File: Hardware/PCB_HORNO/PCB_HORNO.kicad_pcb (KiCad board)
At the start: 2 copper layers, 273 parts, among them J0_1 Screw_Terminal_01x03, J0_10 Screw_Terminal_01x03, J0_13 Screw_Terminal_01x03, J0_14 Screw_Terminal_01x03, J0_16 Screw_Terminal_01x03, J0_18 Screw_Terminal_01x03, J0_19 Screw_Terminal_01x03, J0_2 Screw_Terminal_01x03, J0_20 Screw_Terminal_01x03, J0_21 Screw_Terminal_01x03, J0_22 Screw_Terminal_01x03, J0_23 Screw_Terminal_01x03, J0_24 Screw_Terminal_01x03, J0_25 Screw_Terminal_01x03, J0_26 Screw_Terminal_01x03, J0_3 Screw_Terminal_01x03, J0_5 Screw_Terminal_01x03, J0_6 Screw_Terminal_01x03, J0_7 Screw_Terminal_01x03, J0_8 Screw_Terminal_01x03, J0_9 Screw_Terminal_01x03, J1 Screw_Terminal_01x20, J2 Screw_Terminal_01x20, J3 Screw_Terminal_01x20, J4 Screw_Terminal_01x20, K1 Fujitsu_FTR-LYCA005x, K2 Fujitsu_FTR-LYCA005x, K3 Fujitsu_FTR-LYCA005x, K4 Fujitsu_FTR-LYCA005x, Q1 2N2222, Q2 2N2222, Q3 2N2222, Q4 2N2222, Q5 BTA16-800B, Q6 IRG4PF50W, Q7 IRG4PF50W, U1 TLP521-1, U10 LM741, U11 LM741, U12 LM741, U13 MOC3021M, U14 TLP521-1, U15 TLP250, U16 TLP521-1, U17 LM741, U18 LM741, U19 TLP250, U2 TLP521-1, U20 L298HN, U21 TLP521-1, U22 TLP521-1, U23 TLP521-1, U3 TLP521-1, U4 TLP521-1, U5 TLP521-1, U6 TLP521-1, U7 TLP521-1, U8 TLP521-1, U9 LM741

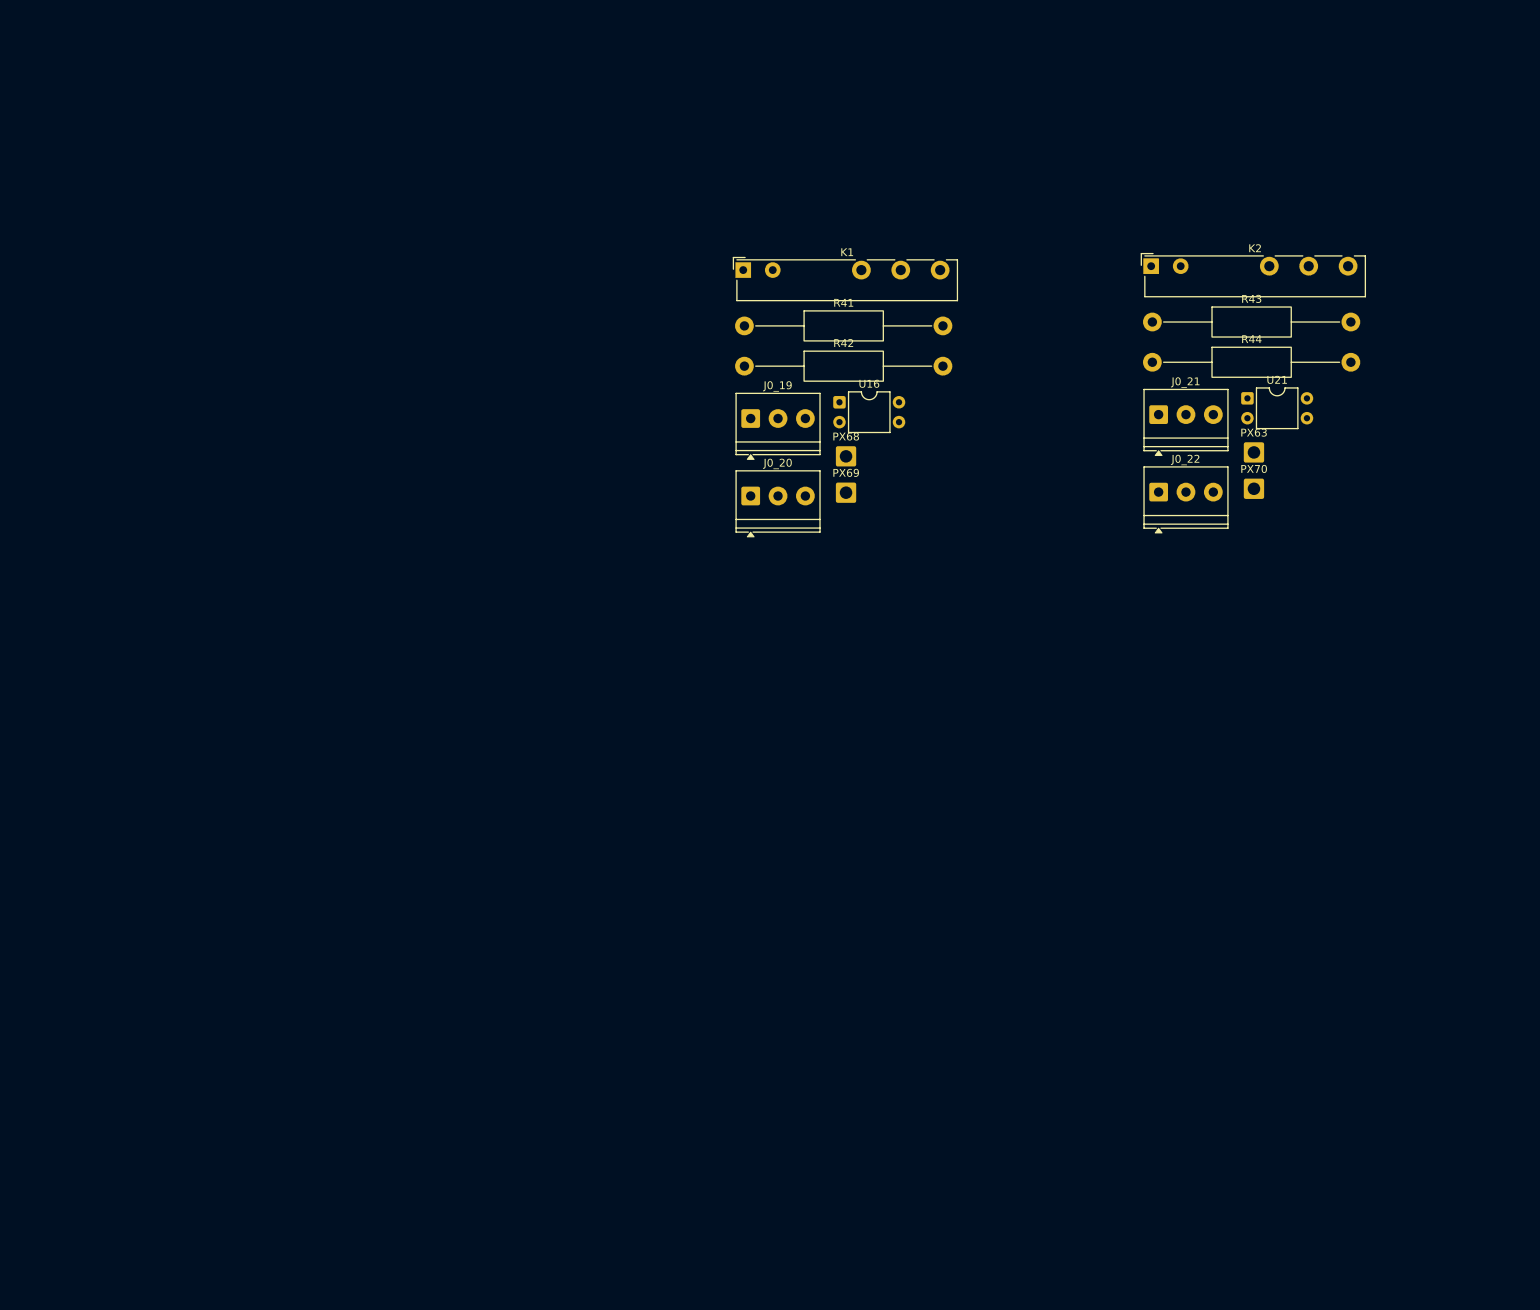
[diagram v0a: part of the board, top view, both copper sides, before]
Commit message: Agregando diodos de rueda libre (flyback)
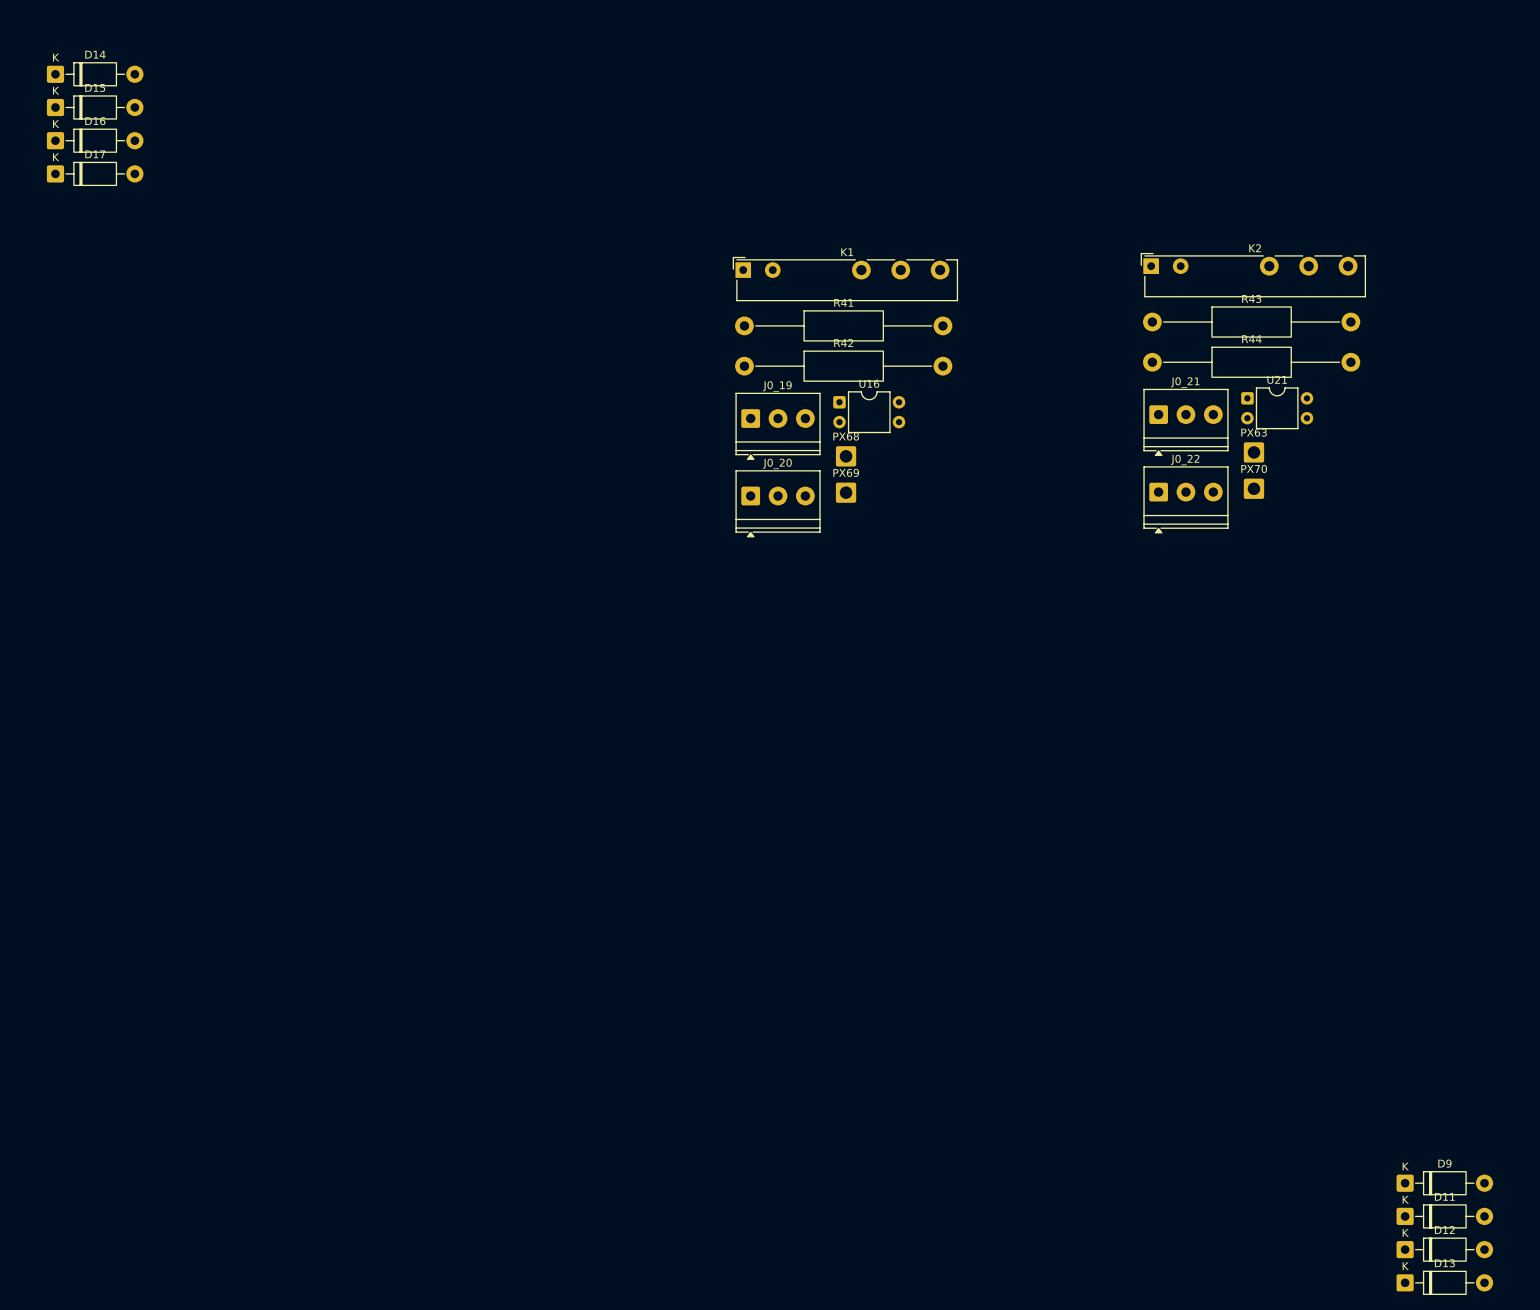
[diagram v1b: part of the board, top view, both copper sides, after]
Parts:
- added D11: 1N4007, Diode_THT:D_DO-41_SOD81_P10.16mm_Horizontal, F.Cu at (146.5, 530.1)
- added D12: 1N4007, Diode_THT:D_DO-41_SOD81_P10.16mm_Horizontal, F.Cu at (146.5, 534.4)
- added D13: 1N4007, Diode_THT:D_DO-41_SOD81_P10.16mm_Horizontal, F.Cu at (146.5, 538.6)
- added D14: 1N4007, Diode_THT:D_DO-41_SOD81_P10.16mm_Horizontal, F.Cu at (-26.2, 383.9)
- added D15: 1N4007, Diode_THT:D_DO-41_SOD81_P10.16mm_Horizontal, F.Cu at (-26.2, 388.2)
- added D16: 1N4007, Diode_THT:D_DO-41_SOD81_P10.16mm_Horizontal, F.Cu at (-26.2, 392.4)
- added D17: 1N4007, Diode_THT:D_DO-41_SOD81_P10.16mm_Horizontal, F.Cu at (-26.2, 396.7)
- added D9: 1N4007, Diode_THT:D_DO-41_SOD81_P10.16mm_Horizontal, F.Cu at (146.5, 525.9)

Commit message: PCB preliminar
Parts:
- RV1: value R_Potentiometer_US -> Potentiometer
- moved J0_5 336.8 mm to (892.9, 343.2), turned to 90 degrees
- moved J0_6 334.0 mm to (892.6, 366.8), turned to 90 degrees
- moved D14 327.8 mm to (297.8, 334.1), turned to 180 degrees
- moved D15 317.8 mm to (287.6, 338.1)
- moved U9 306.7 mm to (836.6, 327.8)
- moved J0_16 305.0 mm to (314.9, 350.4)
- moved C5 304.8 mm to (864.6, 339.4), turned to 90 degrees
- moved D16 304.2 mm to (272.4, 334.2), turned to 180 degrees
- moved C6 302.4 mm to (864.3, 351.5), turned to 90 degrees
- moved C4 295.0 mm to (863.9, 370.8), turned to 90 degrees
- moved D17 294.3 mm to (262.2, 338.1)
- moved J0_10 293.9 mm to (289.3, 350.4)
- moved U10 293.4 mm to (837.4, 344.7)
- moved C10 292.8 mm to (270.3, 304.4)
- moved C11 292.8 mm to (270.3, 312.4)
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
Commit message: Esquematico definitivo
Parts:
- removed D14, D15, D16, D17: 1N4007, Diode_THT:D_DO-41_SOD81_P10.16mm_Horizontal

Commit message: Actualización de esquematico
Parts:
- removed PX116, PX120, PX56, PX58, PX60, PX61, PX64, PX65, PX68, PX70, PX71, PX73, PX74, PX75, PX76, PX77, PX78, PX79, PX81, PX82, PX83, PX84, PX85, PX86, PX87, PX88, PX89, PX90: ~, Connector_Wire:SolderWire-0.75sqmm_1x01_D1.25mm_OD2.3mm
- R1, R12, R14, R15, R16, R17, R18, R19, R2, R20, R21, R22, R23, R24, R25, R26, R3, R35, R36, R37, R38, R4, R41, R44, R46, R48, R49, R5, R6, R7, R8: footprint Resistor_THT:R_Axial_DIN0411_L9.9mm_D3.6mm_P25.40mm_Horizontal -> Resistor_THT:R_Axial_DIN0207_L6.3mm_D2.5mm_P10.16mm_Horizontal
- R13, R27, R28, R29, R30, R31, R32, R33, R34, R39, R40, R42, R43, R45, R47: footprint Resistor_THT:R_Axial_DIN0411_L9.9mm_D3.6mm_P25.40mm_Horizontal -> Resistor_THT:R_Axial_DIN0309_L9.0mm_D3.2mm_P15.24mm_Horizontal
- RV1: value Potentiometer -> R_Potentiometer_US
- moved PX45 641.0 mm to (272.9, 274.6)
- moved J0_5 554.8 mm to (395.6, 97.3), turned to 180 degrees
- moved J0_6 544.6 mm to (419.2, 97.6), turned to 180 degrees
- moved PX55 489.3 mm to (277.5, 274.6)
- moved C3 480.0 mm to (444.7, 151.3), turned to -90 degrees
- moved C4 466.8 mm to (445.0, 165.0), turned to -90 degrees
- moved C6 451.8 mm to (444.6, 184.3), turned to -90 degrees
- moved C5 444.0 mm to (444.3, 196.4), turned to -90 degrees
- moved J0_3 436.5 mm to (-361.2, 28.9), turned to 180 degrees
- moved U12 435.3 mm to (471.0, 150.8), turned to 180 degrees
- moved J0_2 433.9 mm to (-340.9, 28.9), turned to 180 degrees
- moved J0_1 432.8 mm to (-318.7, 29.2), turned to 180 degrees
- moved U11 412.7 mm to (471.4, 172.6), turned to 180 degrees
- moved U10 396.9 mm to (471.5, 191.1), turned to 180 degrees
- moved U9 383.6 mm to (472.2, 208.0), turned to 180 degrees
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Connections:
- C10 pad 1: Net-(J0_16-Pin_1) -> Net-(GND1-Pin_1)
- C11 pad 1: Net-(J0_16-Pin_1) -> Net-(GND1-Pin_1)
- C3 pad 2: Net-(J0_6-Pin_2) -> Net-(GND1-Pin_1)
- C4 pad 2: Net-(J0_6-Pin_2) -> Net-(GND1-Pin_1)
- C5 pad 2: Net-(J0_6-Pin_2) -> Net-(GND1-Pin_1)
- C6 pad 2: Net-(J0_6-Pin_2) -> Net-(GND1-Pin_1)
- C8 pad 2: Net-(J0_6-Pin_2) -> Net-(GND1-Pin_1)
- C9 pad 2: Net-(J0_6-Pin_2) -> Net-(GND1-Pin_1)
- J0_16 pad 1: Net-(J0_16-Pin_1) -> Net-(GND1-Pin_1)
- J0_6 pad 2: Net-(J0_6-Pin_2) -> Net-(GND1-Pin_1)
- J0_6 pad 3: Net-(J0_6-Pin_2) -> Net-(GND1-Pin_1)
- PS1 pad 1: Net-(PS1--Vin) -> Net-(GND1-Pin_1)
- PS1 pad 2: Net-(PS1-+Vin) -> Net-(5Vb1-Pin_1)
- PS2 pad 1: Net-(PS2--Vin) -> Net-(GND1-Pin_1)
- PS2 pad 2: Net-(PS2-+Vin) -> Net-(5Vb1-Pin_1)
- PS3 pad 1: Net-(PS3--Vin) -> Net-(GND1-Pin_1)
- PS3 pad 2: Net-(PS3-+Vin) -> Net-(5Vb1-Pin_1)
- PS4 pad 1: Net-(PS4--Vin) -> Net-(GND1-Pin_1)
- PS4 pad 2: Net-(PS4-+Vin) -> Net-(5Vb1-Pin_1)
- PS5 pad 1: Net-(PS5--Vin) -> Net-(GND1-Pin_1)
- PS5 pad 2: Net-(PS5-+Vin) -> Net-(3V3a1-Pin_1)
- PS5 pad 3: Net-(PS5--Vout) -> Net-(GND1-Pin_1)
- PS6 pad 1: Net-(PS6--Vin) -> Net-(GND1-Pin_1)
- PS6 pad 2: Net-(PS6-+Vin) -> Net-(5Vb1-Pin_1)
- PS6 pad 3: Net-(J0_6-Pin_2) -> Net-(GND1-Pin_1)
- PS7 pad 1: Net-(PS7--Vin) -> Net-(GND1-Pin_1)
- PS7 pad 2: Net-(PS7-+Vin) -> Net-(5Vb1-Pin_1)
- PS7 pad 4: Net-(J0_6-Pin_2) -> Net-(GND1-Pin_1)
- PS8 pad 1: Net-(PS8--Vin) -> Net-(GND1-Pin_1)
- PS8 pad 2: Net-(PS8-+Vin) -> Net-(5Vb1-Pin_1)
- PS8 pad 3: Net-(J0_6-Pin_2) -> Net-(GND1-Pin_1)
- PX45 pad 1: Net-(PS5--Vout) -> Net-(PX45-Pin_1)
- PX46 pad 1: Net-(PS5--Vout) -> Net-(GND1-Pin_1)
- PX55 pad 1: Net-(PS5--Vout) -> Net-(PX55-Pin_1)
- R1 pad 1: Net-(PS5--Vout) -> Net-(GND1-Pin_1)
- R1 pad 2: Net-(PS5--Vout) -> Net-(GND1-Pin_1)
- R2 pad 2: Net-(PS5--Vout) -> Net-(GND1-Pin_1)
- R21 pad 2: Net-(J0_6-Pin_2) -> Net-(GND1-Pin_1)
- R23 pad 2: Net-(J0_6-Pin_2) -> Net-(GND1-Pin_1)
- R3 pad 2: Net-(PS5--Vout) -> Net-(GND1-Pin_1)
- R35 pad 2: Net-(J0_6-Pin_2) -> Net-(GND1-Pin_1)
- R36 pad 2: Net-(J0_6-Pin_2) -> Net-(GND1-Pin_1)
- R37 pad 2: Net-(J0_6-Pin_2) -> Net-(GND1-Pin_1)
- R38 pad 2: Net-(J0_6-Pin_2) -> Net-(GND1-Pin_1)
- R39 pad 1: Net-(J0_16-Pin_1) -> Net-(GND1-Pin_1)
- R4 pad 2: Net-(PS5--Vout) -> Net-(GND1-Pin_1)
- R40 pad 1: Net-(J0_16-Pin_1) -> Net-(GND1-Pin_1)
- R5 pad 2: Net-(PS5--Vout) -> Net-(GND1-Pin_1)
- R6 pad 2: Net-(PS5--Vout) -> Net-(GND1-Pin_1)
- R7 pad 2: Net-(PS5--Vout) -> Net-(GND1-Pin_1)
- R8 pad 2: Net-(PS5--Vout) -> Net-(GND1-Pin_1)
- RV1 pad 1: Net-(PX58-Pin_1) -> Net-(GND1-Pin_1)
- RV1 pad 3: Net-(PX60-Pin_1) -> Net-(3V3a1-Pin_1)
- U1 pad 3: Net-(PS5--Vout) -> Net-(GND1-Pin_1)
- U13 pad 2: Net-(PX56-Pin_1) -> Net-(GND1-Pin_1)
- U14 pad 3: Net-(PS5--Vout) -> Net-(GND1-Pin_1)
- U15 pad 3: Net-(PX65-Pin_1) -> Net-(GND1-Pin_1)
- U16 pad 2: Net-(PX68-Pin_1) -> Net-(GND1-Pin_1)
- U19 pad 3: Net-(PX79-Pin_1) -> Net-(GND1-Pin_1)
- U20 pad 11: unconnected-(U20-EnB-Pad11) -> Net-(PX45-Pin_1)
- U20 pad 6: unconnected-(U20-EnA-Pad6) -> Net-(PX55-Pin_1)
- U20 pad 8: Net-(J0_16-Pin_1) -> Net-(GND1-Pin_1)
- U21 pad 2: Net-(PX70-Pin_1) -> Net-(GND1-Pin_1)
- U22 pad 2: Net-(PX64-Pin_1) -> Net-(GND1-Pin_1)
- U23 pad 2: Net-(PX71-Pin_1) -> Net-(GND1-Pin_1)

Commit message: Actualización de PCB
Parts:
- moved PX118 560.0 mm to (188.1, 118.3), turned to 180 degrees
- moved PX119 556.1 mm to (188.1, 112.8), turned to 180 degrees
- moved R23 531.2 mm to (221.2, 138.7), turned to 90 degrees
- moved R49 530.2 mm to (89.9, 92.7), turned to 180 degrees
- moved C9 520.5 mm to (207.8, 120.5), turned to -90 degrees
- moved U18 507.5 mm to (206.8, 107.6), turned to 90 degrees
- moved R24 502.4 mm to (220.8, 121.2), turned to 90 degrees
- moved R21 498.9 mm to (252.5, 139.7), turned to 90 degrees
- moved R8 494.7 mm to (92.2, 180.5), turned to 0 degrees
- moved PS7 490.3 mm to (221.9, 90.9)
- moved PS8 490.3 mm to (200.0, 91.0)
- moved PS6 490.3 mm to (242.0, 91.3)
- moved C8 488.9 mm to (236.1, 124.4), turned to -90 degrees
- moved PX53 488.9 mm to (109.2, 160.6), turned to 0 degrees
- moved PX52 485.5 mm to (109.2, 156.0), turned to 0 degrees
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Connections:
- J0_13 pad 2: unconnected-(J0_13-Pin_2-Pad2) -> Net-(GND1-Pin_1)
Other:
- board outline added: 256.1 x 296.8 mm

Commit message: Layout del PCB
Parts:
- added REF**: MountingHole_4.5mm_Pad, MountingHole:MountingHole_4.5mm_Pad, F.Cu at (44.5, 268.0)
- added REF**: MountingHole_4.5mm_Pad, MountingHole:MountingHole_4.5mm_Pad, F.Cu at (254.0, 268.0)
- added REF**: MountingHole_4.5mm_Pad, MountingHole:MountingHole_4.5mm_Pad, F.Cu at (254.0, 21.0)
- added REF**: MountingHole_4.5mm_Pad, MountingHole:MountingHole_4.5mm_Pad, F.Cu at (147.8, 117.0)
- added REF**: MountingHole_4.5mm_Pad, MountingHole:MountingHole_4.5mm_Pad, F.Cu at (44.5, 21.0)
- RV1: value R_Potentiometer_US -> Potentiometer
- moved J0_19 33.4 mm to (56.0, 262.8)
- moved J0_21 28.8 mm to (93.0, 262.8)
- moved J0_20 27.1 mm to (71.5, 262.8)
- moved J0_16 26.5 mm to (234.1, 262.7)
- moved K1 25.8 mm to (80.5, 249.8)
- moved D11 25.6 mm to (100.5, 228.8)
- moved J0_10 25.4 mm to (218.1, 262.7)
- moved J0_23 25.2 mm to (130.0, 262.8)
- moved R43 24.9 mm to (92.5, 239.8)
- moved U16 24.5 mm to (73.5, 231.8)
- moved R42 24.5 mm to (55.5, 239.8)
- moved J0_22 24.4 mm to (108.5, 262.8)
- moved R21 24.2 mm to (235.0, 123.0)
- moved J0_26 24.2 mm to (181.5, 262.8)
- moved U21 24.0 mm to (110.5, 231.8)
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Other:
- board size 256.1 x 296.8 mm -> 226.2 x 263.7 mm

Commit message: Ruteo
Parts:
- moved PX10 0.92 mm to (130.6, 146.7)
- moved PX11 0.92 mm to (130.6, 150.7)
- moved PX12 0.92 mm to (130.6, 154.7)
- moved PX13 0.92 mm to (130.6, 158.7)
- moved PX14 0.92 mm to (130.6, 162.7)
- moved PX15 0.92 mm to (130.6, 166.7)
- moved PX16 0.92 mm to (130.6, 170.7)
- moved PX17 0.92 mm to (130.6, 174.7)
- moved PX18 0.92 mm to (130.6, 178.7)
- moved PX19 0.92 mm to (130.6, 182.7)
- moved PX20 0.92 mm to (130.6, 186.7)
- moved PX21 0.92 mm to (130.6, 190.7)
- moved PX22 0.92 mm to (130.6, 194.7)
- moved PX6 0.92 mm to (130.6, 130.7)
- moved PX7 0.92 mm to (130.6, 134.7)
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- renumbered REF** to H1, REF** to H2, REF** to H3, REF** to H4, REF** to H5
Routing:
- net Net-(GND1-Pin_1): track 0.00 -> 1057.3 mm, vias 0 -> 1
- net Net-(5Vb1-Pin_1): track 0.00 -> 235.8 mm, vias 0 -> 1
- net Net-(3V3a1-Pin_1): track 0.00 -> 222.4 mm, vias 0 -> 1
- net Net-(PS6-+Vout): track 0.00 -> 153.5 mm, vias 0 -> 1
- net Net-(PS7--Vout): track 0.00 -> 140.7 mm, vias 0 -> 1
- net Net-(J0_1-Pin_1): track 0.00 -> 132.3 mm
- net Net-(R49-Pad2): track 0.00 -> 104.2 mm
- net Net-(J0_14-Pin_3): track 0.00 -> 90.4 mm
- net Net-(J0_18-Pin_3): track 0.00 -> 89.1 mm, vias 0 -> 1
- net Net-(J0_5-Pin_1): track 0.00 -> 82.2 mm
- net Net-(PS8-+Vout): track 0.00 -> 73.3 mm
- net Net-(J0_13-Pin_1): track 0.00 -> 69.8 mm, vias 0 -> 1
- net Net-(J0_5-Pin_2): track 0.00 -> 68.4 mm
- net Net-(J0_9-Pin_1): track 0.00 -> 67.2 mm, vias 0 -> 1
- net Net-(PS5-+Vout): track 0.00 -> 62.4 mm
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
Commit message: Ruteo de PCB
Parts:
- RV1: value Potentiometer -> R_Potentiometer_US
- moved PX62 21.5 mm to (237.0, 212.0)
- moved J0_6 19.4 mm to (251.9, 40.6)
- moved J0_5 19.4 mm to (252.0, 60.0)
- moved R40 17.1 mm to (200.6, 251.0)
- moved PX55 17.0 mm to (227.7, 212.0)
- moved U20 15.4 mm to (227.3, 243.7), turned to 0 degrees
- moved C11 15.4 mm to (210.3, 234.8)
- moved PX112 14.1 mm to (210.7, 212.0)
- moved PX113 14.1 mm to (215.3, 212.0)
- moved C5 14.0 mm to (207.0, 22.6)
- moved C6 14.0 mm to (193.0, 22.7)
- moved PX111 12.3 mm to (232.4, 212.0)
- moved R23 10.0 mm to (204.9, 113.0), turned to -90 degrees
- moved R24 10.0 mm to (204.9, 95.0), turned to -90 degrees
- moved R21 10.0 mm to (235.0, 113.0), turned to -90 degrees
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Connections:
- C2 pad 2: Net-(GND3-Pin_1) -> Net-(GND1-Pin_1)
- GND3 pad 1: Net-(GND3-Pin_1) -> Net-(GND1-Pin_1)
- J4 pad 20: Net-(GND3-Pin_1) -> Net-(GND1-Pin_1)
- PS8 pad 2: Net-(5Vb1-Pin_1) -> Net-(3V3b1-Pin_1)
- PX46 pad 1: Net-(GND1-Pin_1) -> Net-(PX46-Pin_1)
- R1 pad 1: Net-(GND1-Pin_1) -> Net-(PX46-Pin_1)
- U1 pad 3: Net-(GND1-Pin_1) -> Net-(PX46-Pin_1)
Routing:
- net Net-(GND1-Pin_1): track 1057.3 -> 1206.6 mm, vias 1 -> 3
- net Net-(PS6-+Vout): track 153.5 -> 217.4 mm, vias 1 -> 0
- net Net-(3V3b1-Pin_1): track 53.2 -> 98.5 mm
- net Net-(PX112-Pin_1): track 25.9 -> 69.5 mm, vias 0 -> 1
- net Net-(GND3-Pin_1): track 35.5 -> 0.00 mm
- net Net-(PX45-Pin_1): track 43.0 -> 78.3 mm
- net Net-(PX113-Pin_1): track 21.6 -> 49.7 mm, vias 0 -> 1
- net Net-(J0_9-Pin_3): track 56.4 -> 31.1 mm, vias 1 -> 0
- net Net-(U20-SENSE_B): track 23.6 -> 48.8 mm, vias 1 -> 0
- net Net-(PX46-Pin_1): track 0.00 -> 23.3 mm
- net Net-(U18--): track 45.5 -> 24.2 mm
- net Net-(U17--): track 45.5 -> 24.3 mm
- net Net-(J0_10-Pin_1): track 30.2 -> 50.0 mm
- net Net-(5Vb1-Pin_1): track 235.8 -> 254.0 mm, vias 1 -> 0
- net Net-(PS8-+Vout): track 73.3 -> 91.1 mm
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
